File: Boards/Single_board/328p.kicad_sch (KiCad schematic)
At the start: 4 parts, among them U2 ATmega328P-A

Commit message: Single board nearly ready to order
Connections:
- net UC_RX: now reaches U2.30 (PD0)
- net UC_TX: now reaches U2.31 (PD1)
- net 328P_RESET renamed RESET
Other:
- moved on the sheet: C3, C4, C5, U2

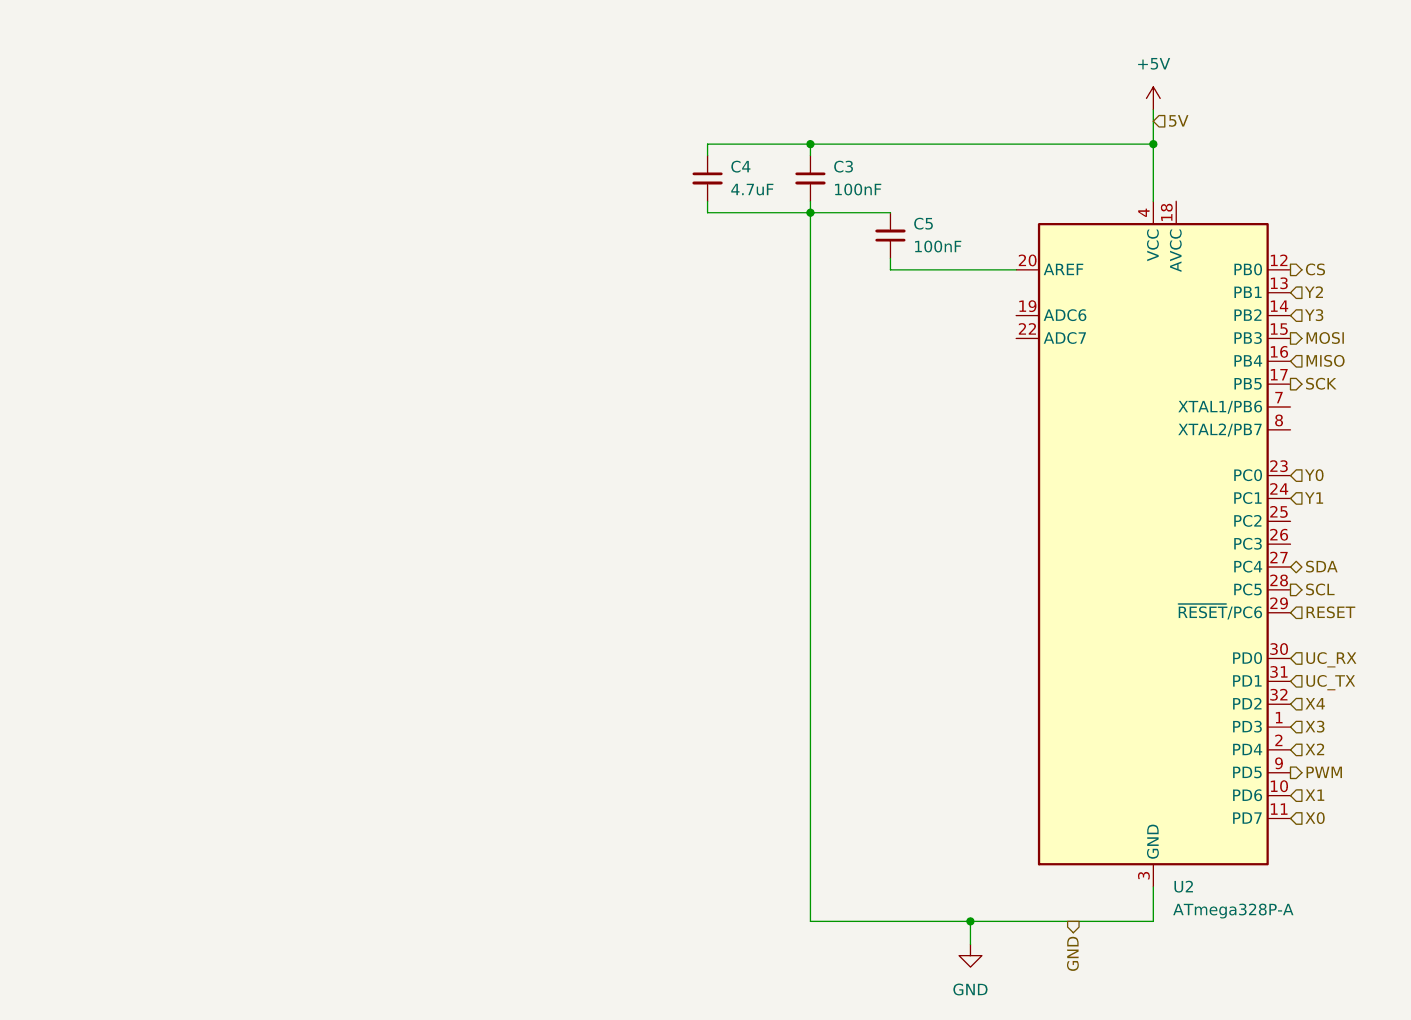
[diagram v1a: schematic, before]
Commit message: Re-stitch and clean up redundant tracks.  Correct some port directions.
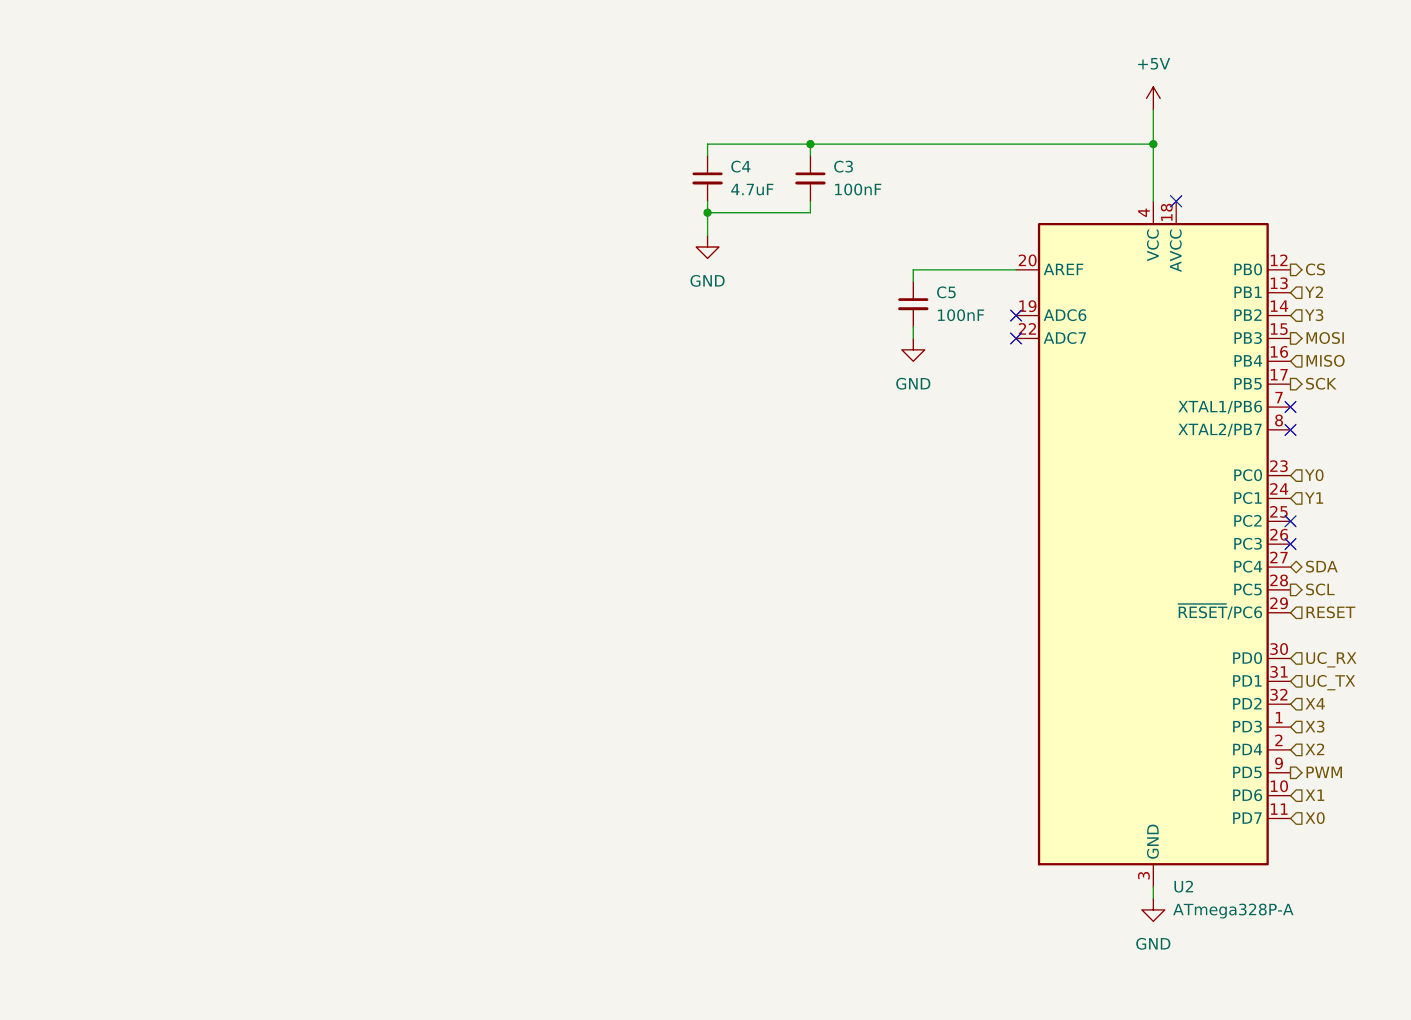
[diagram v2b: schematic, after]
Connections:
- no-connect marks 0 -> 7
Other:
- moved on the sheet: C5

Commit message: Connect AVCC to VCC
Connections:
- net +5V: now also U2.18 (AVCC)
- no-connect marks 7 -> 6
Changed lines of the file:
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@@
 		(at 167.64 88.9)
-	)
-	(no_connect
-		(at 154.94 50.8)
 	)
 	(wire
@@
 		(pts
 			(xy 114.3 50.8) (xy 114.3 52.07)
-		)
-		(stroke
-			(width 0)
-			(type default)
-		)
-	)
-	(wire
-		(pts
-			(xy 152.4 44.45) (xy 152.4 50.8)
 		)
 		(stroke
@@
 	(wire
 		(pts
+			(xy 152.4 44.45) (xy 152.4 50.8)
+		)
+		(stroke
+			(width 0)
+			(type default)
+		)
+	)
+	(wire
+		(pts
+			(xy 154.94 44.45) (xy 152.4 44.45)
+		)
+		(stroke
+			(width 0)
+			(type default)
+		)
+	)
+	(wire
+		(pts
 			(xy 102.87 52.07) (xy 102.87 54.61)
 		)
 		(stroke
+			(width 0)
+			(type default)
+		)
+	)
+	(wire
+		(pts
+			(xy 154.94 50.8) (xy 154.94 44.45)
+		)
+		(stroke

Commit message: Start RGB LED + hotswap socket redesign of single board
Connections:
- net PWM renamed RGB_DIN
- net SCL: no longer names the net of U2.28 (PC5)
- net SDA: no longer names the net of U2.27 (PC4)
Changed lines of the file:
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@@
-		)
-	)
-	(hierarchical_label "SCL"
-		(shape output)
-		(at 167.64 93.98 0)
-		(fields_autoplaced yes)
-		(effects
-			(font
-				(size 1.27 1.27)
-			)
-			(justify left)
 		)
 	)
@@
 		(shape input)
 		(at 167.64 109.22 0)
+		(fields_autoplaced yes)
+		(effects
+			(font
+				(size 1.27 1.27)
+			)
+			(justify left)
+		)
+	)
+	(hierarchical_label "RGB_DIN"
+		(shape output)
+		(at 167.64 114.3 0)
 		(fields_autoplaced yes)
 		(effects
@@
 		)
 	)
-	(hierarchical_label "SDA"
-		(shape bidirectional)
-		(at 167.64 91.44 0)
-		(fields_autoplaced yes)
-		(effects
-			(font
-				(size 1.27 1.27)
-			)
-			(justify left)
-		)
-	)
 	(hierarchical_label "Y0"
 		(shape input)
@@
 		(fields_autoplaced yes)
 		(effects
-			(font
-				(size 1.27 1.27)
-			)
-			(justify left)
-		)
-	)
-	(hierarchical_label "PWM"
-		(shape output)
-		(at 167.64 114.3 0)
-		(fields_autoplaced yes)
-		(effects

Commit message: Arrange and place components
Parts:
- renumbered C4 to C5, C3 to C6, C5 to C7
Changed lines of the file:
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@@
 		(dnp no)
 		(fields_autoplaced yes)
-		(property "Reference" "C3"
+		(property "Reference" "C6"
 			(at 116.84 46.9962 0)
 			(effects
@@
 			(project "Single_board"
 				(path "/f30854c1-5bc2-470d-aabe-1768a5b01b46/10d1b3d3-799b-4f50-9dbd-cebbf84933bb"
-					(reference "C3")
+					(reference "C6")
 					(unit 1)
 				)
@@
 		(dnp no)
 		(fields_autoplaced yes)
-		(property "Reference" "C5"
+		(property "Reference" "C7"
 			(at 128.27 60.9662 0)
 			(effects
@@
 			(project "Single_board"
 				(path "/f30854c1-5bc2-470d-aabe-1768a5b01b46/10d1b3d3-799b-4f50-9dbd-cebbf84933bb"
-					(reference "C5")
+					(reference "C7")
 					(unit 1)
 				)
@@
 		(dnp no)
 		(fields_autoplaced yes)
-		(property "Reference" "C4"
+		(property "Reference" "C5"
 			(at 105.41 46.9962 0)
 			(effects
@@
 			(project "Single_board"
 				(path "/f30854c1-5bc2-470d-aabe-1768a5b01b46/10d1b3d3-799b-4f50-9dbd-cebbf84933bb"
-					(reference "C4")
-					(unit 1)
-				)
+					(reference "C5")
+					(unit 1)
+				)

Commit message: Add usb ports and separate power sources. Pending fitting test.
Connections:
- net +5V renamed VCC

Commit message: Small routing improvements and prepare for JLC order
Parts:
- C5: footprint Capacitor_SMD:C_0805_2012Metric -> Project Libraries:0805 4.7uF
- C6, C7: footprint Capacitor_SMD:C_0805_2012Metric -> Project Libraries:0805 100nF
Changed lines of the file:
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@@
 			)
 		)
-		(property "Footprint" "Capacitor_SMD:C_0805_2012Metric"
+		(property "Footprint" "Project Libraries:0805 100nF"
 			(at 114.3 48.26 0)
 			(effects
@@
 			)
 		)
-		(property "Footprint" "Capacitor_SMD:C_0805_2012Metric"
+		(property "Footprint" "Project Libraries:0805 100nF"
 			(at 125.73 62.23 0)
 			(effects
@@
 			)
 		)
-		(property "Footprint" "Capacitor_SMD:C_0805_2012Metric"
+		(property "Footprint" "Project Libraries:0805 4.7uF"
 			(at 102.87 48.26 0)
 			(effects
